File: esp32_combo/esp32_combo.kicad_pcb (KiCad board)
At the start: 2 copper layers, 90 x 43 mm, 34 parts, among them J1 TERM BLK 3.5MM 2P SIDE, J2 TERM BLK 3.5MM 6P SIDE, J3 TERM BLK 3.5MM 6P SIDE, J4 TERM BLK 3.5MM 3P SIDE, J5 TERM BLK 3.5MM 3P SIDE, J6 HDR SKT 5PIN VERT 2.54MM, J7 HDR SKT 7PIN VERT 2.54MM, J8 SKT 2x6PIN VERT 2.54MM, J9 HDR SKT 8PIN VERT 2.54MM, Q1 AS2302, SW1 SS12D10, U1 TB6612FNG Module, U2 ESP32 DEV KIT Module 30-pin, U3 LM2596 Module

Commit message: Logo
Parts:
- added G***: LOGO, Makerspet:Maker's Pet Logo 7mm, F.Cu at (58.1, 48.3)
- added G***: LOGO, Makerspet:Maker's Pet Logo 7mm, B.Cu at (120.0, 40.2)
- J7: value HDR SKT 7PIN VERT 2.54MM -> HDR SKT 6PIN VERT 2.54MM; footprint Connector_PinSocket_2.54mm:PinSocket_1x07_P2.54mm_Vertical -> Connector_PinSocket_2.54mm:PinSocket_1x06_P2.54mm_Vertical
- moved SW1 2.67 mm to (62.4, 33.4)
- moved D2 2.62 mm to (54.1, 35.3)
- moved F1 2.62 mm to (51.8, 35.2)
- moved D1 2.59 mm to (71.8, 37.0)
- moved J7 2.54 mm to (71.3, 34.0)
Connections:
- net Net-(D3-A) renamed /MOT
- J7 pad 2: GND -> +5V
- J7 pad 3: +5V -> /GPIO27
- J7 pad 4: /GPIO27 -> /GPIO18
- J7 pad 5: /GPIO18 -> /GPIO5_BOOT_STRAP
- J7 pad 6: /GPIO5_BOOT_STRAP -> /GPIO4
- J9 pad 5: Net-(J9-Pin_5) -> /LDS_PWM
- J9 pad 6: /LDS_PWM -> /LDS_EN
- J9 pad 7: /LDS_RX -> Net-(J9-Pin_7)
- J9 pad 8: /LDS_EN -> /LDS_RX
- R11 pad 2: Net-(J9-Pin_5) -> Net-(J9-Pin_7)
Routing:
- net Net-(J9-Pin_7): track 0.00 -> 32.0 mm
- net Net-(J9-Pin_5): track 27.4 -> 0.00 mm
- net /LDS_EN: track 28.3 -> 17.1 mm
- net Vdrive: track 145.3 -> 142.7 mm
- net Net-(D1-K): track 29.0 -> 31.6 mm
- net Net-(J1-Pin_1): track 6.45 -> 8.73 mm
- net /LDS_RX: track 28.4 -> 30.2 mm
- net +5V: track 242.2 -> 240.5 mm
- net /LDS_PWM: track 61.2 -> 62.6 mm
- net /GPIO27: track 27.2 -> 27.8 mm
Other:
- board text added: "- BAT +"
- board text added: "COMBO"
- board text added: "EN"
- board text added: "INT"
- board text added: "MOT"
- board text added: "R1 ©2024"
- board text added: "RX"
- board text added: "SCL"
- board text added: "SDA"
- board text added: "TX"
- board text added: "U/S SENSOR"
- board text removed: "+BAT"
- board text removed: "Combo v0.1.0"
- board text removed: "U/S DIST SENSOR"

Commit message: Combo tweaks
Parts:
- removed C2: 100uF 16V, Capacitor_Tantalum_SMD:CP_EIA-7343-15_Kemet-W
- C1: value 22uF -> 22uF 6.3V
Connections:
- net /EA_LEFT renamed /EA_LEFT_FG
- net /EA_RIGHT renamed /EA_RIGHT_FG
- net /ENC_A_LEFT renamed /ENC_A_LEFT_FG
- net /ENC_A_RIGHT renamed /ENC_A_RIGHT_FG
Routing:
- net GND: track 9.26 -> 4.78 mm
- net Vdrive: track 142.7 -> 138.7 mm
- net +5V: track 240.5 -> 244.4 mm
- net /LDS_EN: track 17.1 -> 15.9 mm
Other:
- board text added: "EA/FG"
- board text added: "FG/EA"
- board text added: "Max 13.5V 1.2A avg per motor"
- board text removed: "EA"

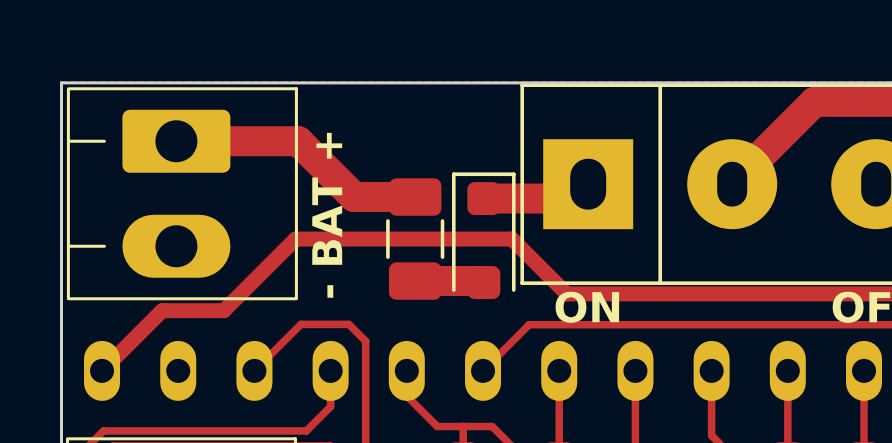
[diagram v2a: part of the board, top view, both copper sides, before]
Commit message: Fuse silkscreen
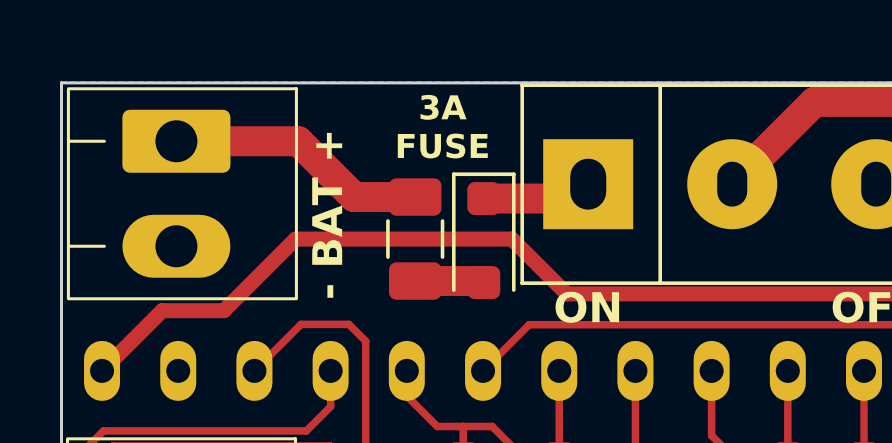
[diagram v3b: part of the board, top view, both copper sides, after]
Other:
- board text added: "3A FUSE"
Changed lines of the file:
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@@
+		)
+	)
+	(gr_text "3A\nFUSE"
+		(at 52.7 32.6 0)
+		(layer "F.SilkS" knockout)
+		(effects
+			(font
+				(size 0.8 0.8)
+				(thickness 0.15)
+				(bold yes)
+			)
+			(justify bottom)
 		)
 	)

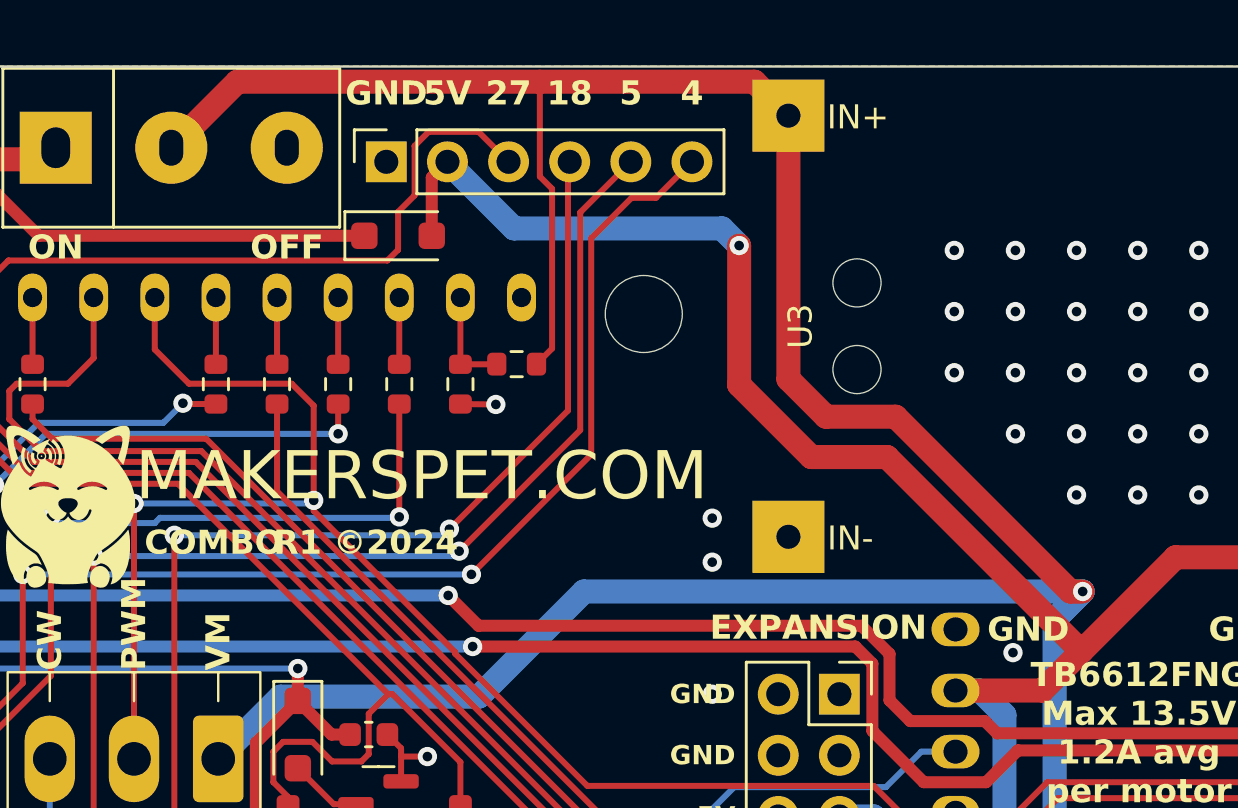
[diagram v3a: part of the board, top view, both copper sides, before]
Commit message: 3A diode
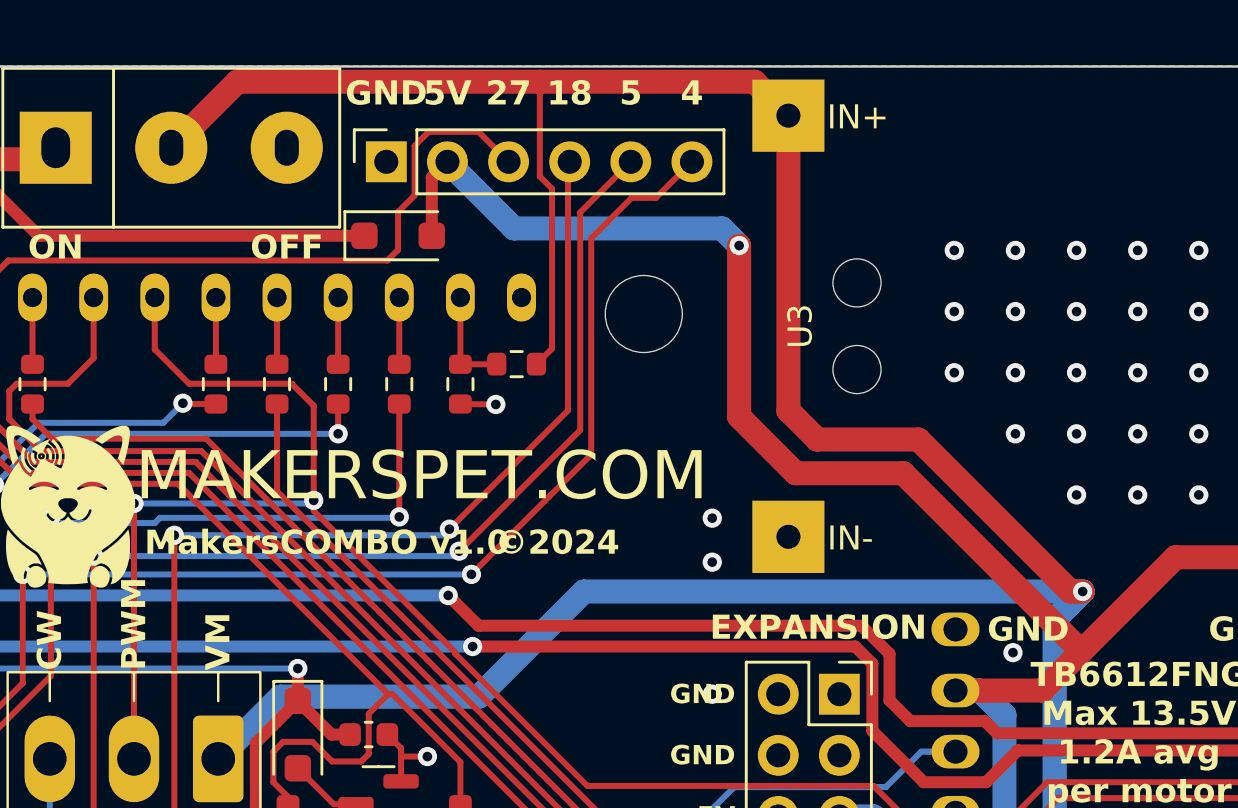
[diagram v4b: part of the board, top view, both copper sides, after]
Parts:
- D2: value FS26 -> FS36
- R5: value 200k -> 200k 1%
- R6: value 20k -> 20k 1%
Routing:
- net +5V: track 244.4 -> 245.2 mm
- net Vdrive: track 138.7 -> 139.4 mm
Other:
- board text added: "MakersCOMBO v1.0"
- board text added: "©2024"
- board text removed: "COMBO"
- board text removed: "R1 ©2024"
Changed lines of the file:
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@@
 	(paper "A5")
 	(title_block
-		(title "ESP32 Combo PCB")
-		(date "2024-04-05")
-		(rev "0.1.0")
+		(title "MakerCombo")
+		(date "2024-04-23")
+		(rev "v1.1.0")
 		(company "makerspet.com")
 	)
@@
 			)
 		)
-		(property "Value" "200k"
+		(property "Value" "200k 1%"
 			(at 0 1.43 0)
 			(layer "F.Fab")
@@
 			)
 		)
-		(property "Value" "FS26"
+		(property "Value" "FS36"
 			(at 0 2.1 90)
 			(layer "F.Fab")
@@
 			)
 		)
-		(property "Datasheet" "https://www.digikey.com/en/products/detail/good-ark-semiconductor/FS26/18667798"
+		(property "Datasheet" "https://www.digikey.com/en/products/detail/good-ark-semiconductor/FS36/18648966"
 			(at 0 0 -90)
 			(unlocked yes)
@@
 			)
 		)
-		(property "Value" "20k"
+		(property "Value" "20k 1%"
 			(at 0 1.43 90)
 			(layer "F.Fab")
@@
 		(layer "Edge.Cuts")
 	)
-	(gr_text "COMBO  "
+	(gr_text "MakersCOMBO v1.0"
 		(at 116.586 41.91 0)
 		(layer "B.SilkS" knockout)
@@
 		)
 	)
-	(gr_text "R1 ©2024"
-		(at 111.2266 41.91 0)
+	(gr_text "©2024"
+		(at 102 41.91 0)
 		(layer "B.SilkS")
 		(effects
@@
 		)
 	)
-	(gr_text "R1 ©2024"
-		(at 66.5988 50.3682 0)
+	(gr_text "©2024"
+		(at 75.8 50.3682 0)
 		(layer "F.SilkS")
 		(effects
@@
 		)
 	)
-	(gr_text "COMBO  "
+	(gr_text "MakersCOMBO v1.0"
 		(at 61.2394 50.3682 0)
 		(layer "F.SilkS" knockout)
@@
 	)
 	(segment
-		(start 73.1804 37.0332)
-		(end 73.1804 34.6122)
-		(width 0.5)
+		(start 88.3 46.9)
+		(end 92.7724 46.9)
+		(width 1)
 		(layer "F.Cu")
 		(net 1)
 	)
 	(segment
-		(start 85.9536 37.4396)
-		(end 85.9536 43.2308)
-		(width 1)
+		(start 73.1804 37.0332)
+		(end 73.1804 34.6122)
+		(width 0.5)
 		(layer "F.Cu")
 		(net 1)
@@
 	)
 	(segment
-		(start 92.1004 46.228)
-		(end 100.1776 54.3052)
-		(width 1)
-		(layer "F.Cu")
-		(net 1)
-	)
-	(segment
 		(start 51.9176 53.389)
 		(end 48.4614 53.389)
@@
 	)
 	(segment
+		(start 85.9536 37.4396)
+		(end 85.9536 44.5536)
+		(width 1)
+		(layer "F.Cu")
+		(net 1)
+	)
+	(segment
 		(start 67.1 66.6)
 		(end 66.3 66.6)
@@
 	)
 	(segment
+		(start 92.7724 46.9)
+		(end 100.1776 54.3052)
+		(width 1)
+		(layer "F.Cu")
+		(net 1)
+	)
+	(segment
 		(start 108.1024 67.9704)
 		(end 108.1024 67.31)
@@
 	)
 	(segment
-		(start 85.9536 43.2308)
-		(end 88.9508 46.228)
+		(start 85.9536 44.5536)
+		(end 88.3 46.9)
 		(width 1)
 		(layer "F.Cu")
@@
 	)
 	(segment
-		(start 88.9508 46.228)
-		(end 92.1004 46.228)
-		(width 1)
-		(layer "F.Cu")
-		(net 1)
-	)
-	(segment
 		(start 108.1024 67.31)
 		(end 106.6292 65.8368)
@@
 	)
 	(segment
-		(start 99.7204 51.816)
-		(end 92.456 44.5516)
+		(start 93.4044 45.5)
+		(end 89.2 45.5)
 		(width 1)
 		(layer "F.Cu")
@@
 	)
 	(segment
-		(start 92.456 44.5516)
-		(end 89.5604 44.5516)
+		(start 99.0654 70.9222)
+		(end 100.5332 72.39)
 		(width 1)
 		(layer "F.Cu")
@@
 	)
 	(segment
-		(start 99.0654 70.9222)
-		(end 100.5332 72.39)
+		(start 99.7204 51.816)
+		(end 93.4044 45.5)
 		(width 1)
 		(layer "F.Cu")
@@
 	)
 	(segment
-		(start 88.0008 42.992)
-		(end 88.0008 32.0424)
-		(width 1)
-		(layer "F.Cu")
-		(net 7)
-	)
-	(segment
 		(start 77.6732 30.6324)
 		(end 86.5908 30.6324)
@@
 	)
 	(segment
-		(start 100.2284 51.816)
-		(end 99.7204 51.816)
+		(start 88.0008 44.3008)
+		(end 88.0008 32.0424)
+		(width 1)
+		(layer "F.Cu")
+		(net 7)
+	)
+	(segment
+		(start 89.2 45.5)
+		(end 88.0008 44.3008)
 		(width 1)
 		(layer "F.Cu")
@@
 	)
 	(segment
-		(start 89.5604 44.5516)
-		(end 88.0008 42.992)
+		(start 99.0654 69.1436)
+		(end 99.0654 70.9222)
 		(width 1)
 		(layer "F.Cu")
@@
 	)
 	(segment
-		(start 99.0654 69.1436)
-		(end 99.0654 70.9222)
+		(start 100.2284 51.816)
+		(end 99.7204 51.816)
 		(width 1)
 		(layer "F.Cu")

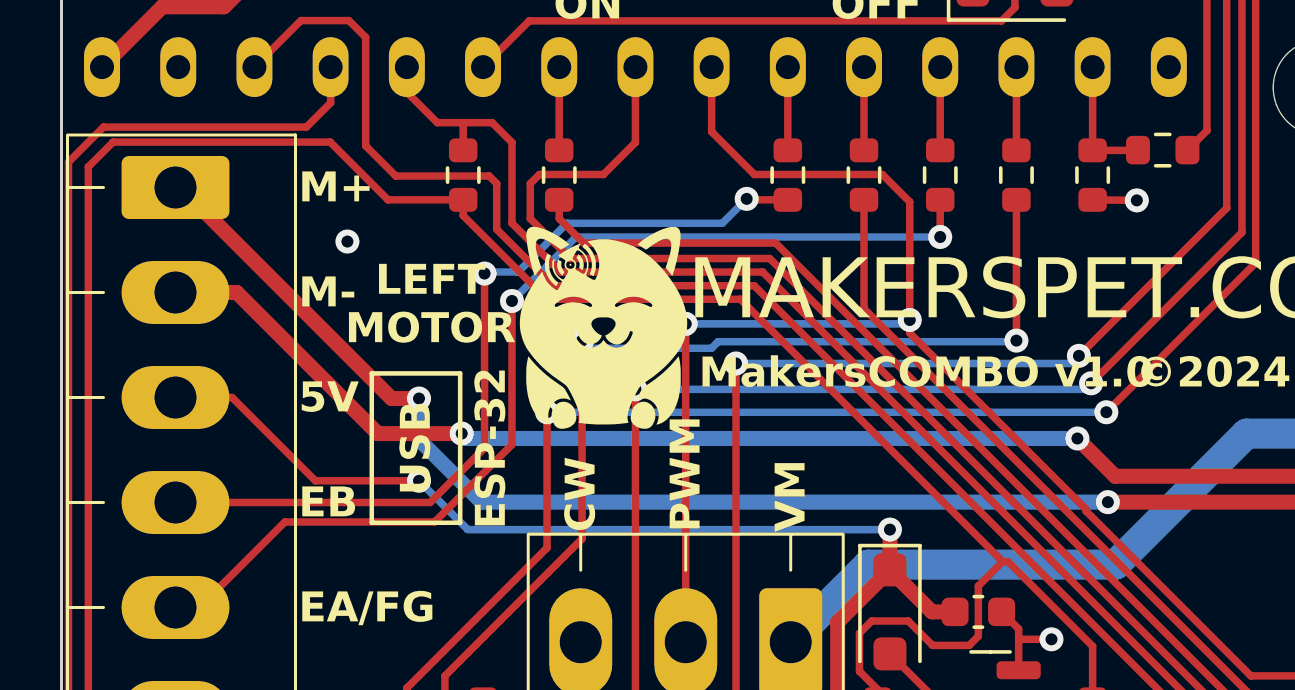
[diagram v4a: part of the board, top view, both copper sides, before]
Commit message: Motor direction bugfix
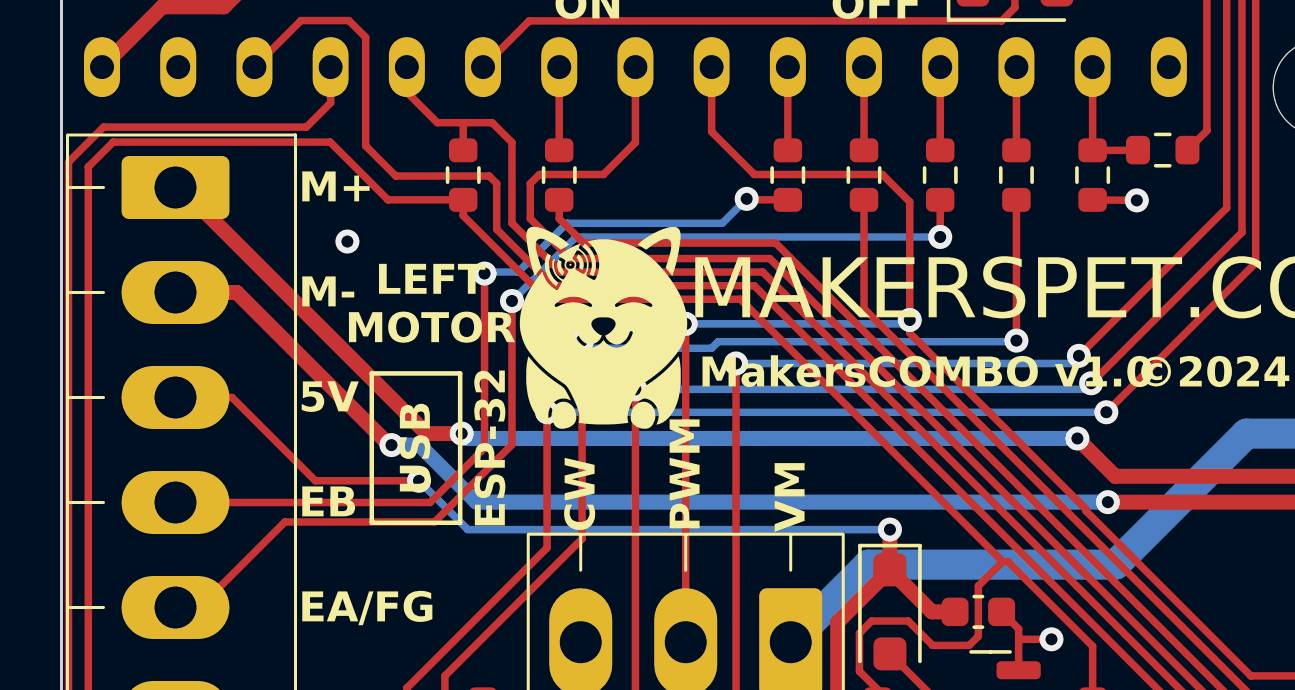
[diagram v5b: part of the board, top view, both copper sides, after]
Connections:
- U1 pad 6: /M+LEFT -> /M-LEFT
- U1 pad 7: /M-LEFT -> /M+LEFT
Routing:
- net /M+LEFT: track 76.1 -> 74.1 mm
- net /M-LEFT: track 72.6 -> 73.8 mm
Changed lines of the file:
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@@
 			(layers "*.Cu" "*.Mask")
 			(remove_unused_layers no)
-			(net 8 "/M+LEFT")
+			(net 9 "/M-LEFT")
 			(pinfunction "B02")
 			(pintype "bidirectional")
@@
 			(layers "*.Cu" "*.Mask")
 			(remove_unused_layers no)
-			(net 9 "/M-LEFT")
+			(net 8 "/M+LEFT")
 			(pinfunction "B01")
 			(pintype "passive")
@@
 	)
 	(segment
-		(start 91.4908 54.8132)
-		(end 91.4908 57.6072)
+		(start 91.0336 53.2384)
+		(end 92.202 54.4068)
 		(width 0.5)
 		(layer "F.Cu")
@@
 	)
 	(segment
-		(start 96.2152 59.7408)
-		(end 97.536 58.42)
+		(start 73.8632 51.979599)
+		(end 75.122001 53.2384)
 		(width 0.5)
 		(layer "F.Cu")
@@
 	)
 	(segment
-		(start 97.536 58.42)
-		(end 110.1344 58.42)
+		(start 96.6724 57.7088)
+		(end 108.4072 57.7088)
 		(width 0.5)
 		(layer "F.Cu")
@@
 	)
 	(segment
-		(start 74.8792 54.102)
-		(end 90.7796 54.102)
+		(start 108.4072 57.7088)
+		(end 110.1852 55.9308)
 		(width 0.5)
 		(layer "F.Cu")
@@
 	)
 	(segment
-		(start 51.9176 50.6476)
-		(end 51.8668 50.6476)
+		(start 92.202 56.3372)
+		(end 93.0656 57.2008)
 		(width 0.5)
 		(layer "F.Cu")
@@
 	)
 	(segment
-		(start 43.9691 43.6135)
-		(end 51.0032 50.6476)
+		(start 96.1644 57.2008)
+		(end 96.6724 57.7088)
 		(width 0.5)
 		(layer "F.Cu")
@@
 	)
 	(segment
-		(start 91.4908 57.6072)
-		(end 93.6244 59.7408)
+		(start 75.122001 53.2384)
+		(end 91.0336 53.2384)
 		(width 0.5)
 		(layer "F.Cu")
@@
 	)
 	(segment
-		(start 90.7796 54.102)
-		(end 91.4908 54.8132)
+		(start 92.202 54.4068)
+		(end 92.202 56.3372)
 		(width 0.5)
 		(layer "F.Cu")
@@
 	)
 	(segment
-		(start 43.8 43.6135)
-		(end 43.9691 43.6135)
+		(start 52.1716 51.816)
+		(end 53.34 51.816)
 		(width 0.5)
 		(layer "F.Cu")
@@
 	)
 	(segment
-		(start 93.6244 59.7408)
-		(end 96.2152 59.7408)
+		(start 93.0656 57.2008)
+		(end 96.1644 57.2008)
 		(width 0.5)
 		(layer "F.Cu")
@@
 	)
 	(segment
-		(start 110.1344 58.42)
-		(end 110.1852 58.4708)
+		(start 43.8 43.6135)
+		(end 43.9691 43.6135)
 		(width 0.5)
 		(layer "F.Cu")
@@
 	)
 	(segment
-		(start 51.0032 50.6476)
-		(end 51.9176 50.6476)
+		(start 43.9691 43.6135)
+		(end 52.1716 51.816)
 		(width 0.5)
 		(layer "F.Cu")
@@
 	)
 	(via
-		(at 51.9176 50.6476)
+		(at 73.8632 51.979599)
 		(size 0.8)
 		(drill 0.4)
@@
 	)
 	(via
-		(at 74.8792 54.102)
+		(at 53.34 51.816)
 		(size 0.8)
 		(drill 0.4)
@@
 	)
 	(segment
-		(start 54.0004 54.102)
-		(end 51.9176 52.0192)
-		(width 0.5)
+		(start 53.3538 51.8298)
+		(end 53.34 51.816)
+		(width 0.25)
 		(layer "B.Cu")
 		(net 8)
 	)
 	(segment
-		(start 51.9176 52.0192)
-		(end 51.9176 50.6476)
+		(start 53.503599 51.979599)
+		(end 53.3538 51.8298)
 		(width 0.5)
 		(layer "B.Cu")
@@
 	)
 	(segment
-		(start 74.8792 54.102)
-		(end 54.0004 54.102)
+		(start 73.8632 51.979599)
+		(end 53.503599 51.979599)
 		(width 0.5)
 		(layer "B.Cu")
@@
 	)
 	(segment
-		(start 91.0336 53.2384)
-		(end 92.202 54.4068)
-		(width 0.5)
-		(layer "F.Cu")
-		(net 9)
-	)
-	(segment
-		(start 45.8435 47.1135)
-		(end 43.8 47.1135)
+		(start 91.4908 54.8132)
+		(end 91.4908 57.6072)
 		(width 0.5)
 		(layer "F.Cu")
@@
 	)
 	(segment
-		(start 73.8632 51.979599)
-		(end 75.122001 53.2384)
+		(start 96.2152 59.7408)
+		(end 97.536 58.42)
 		(width 0.5)
 		(layer "F.Cu")
@@
 	)
 	(segment
-		(start 96.6724 57.7088)
-		(end 108.4072 57.7088)
+		(start 97.536 58.42)
+		(end 110.1344 58.42)
 		(width 0.5)
 		(layer "F.Cu")
@@
 	)
 	(segment
-		(start 108.4072 57.7088)
-		(end 110.1852 55.9308)
+		(start 74.8792 54.102)
+		(end 90.7796 54.102)
 		(width 0.5)
 		(layer "F.Cu")
@@
 	)
 	(segment
-		(start 92.202 56.3372)
-		(end 93.0656 57.2008)
+		(start 91.4908 57.6072)
+		(end 93.6244 59.7408)
 		(width 0.5)
 		(layer "F.Cu")
@@
 	)
 	(segment
-		(start 96.1644 57.2008)
-		(end 96.6724 57.7088)
+		(start 50.93 52.2)
+		(end 45.8435 47.1135)
 		(width 0.5)
 		(layer "F.Cu")
@@
 	)
 	(segment
-		(start 75.122001 53.2384)
-		(end 91.0336 53.2384)
+		(start 90.7796 54.102)
+		(end 91.4908 54.8132)
 		(width 0.5)
 		(layer "F.Cu")
@@
 	)
 	(segment
-		(start 92.202 54.4068)
-		(end 92.202 56.3372)
+		(start 93.6244 59.7408)
+		(end 96.2152 59.7408)
 		(width 0.5)
 		(layer "F.Cu")
@@
 	)
 	(segment
-		(start 93.0656 57.2008)
-		(end 96.1644 57.2008)
+		(start 45.8435 47.1135)
+		(end 43.8 47.1135)
 		(width 0.5)
 		(layer "F.Cu")
@@
 	)
 	(segment
-		(start 50.546 51.816)
-		(end 45.8435 47.1135)
+		(start 110.1344 58.42)
+		(end 110.1852 58.4708)
 		(width 0.5)
 		(layer "F.Cu")
@@
 	)
 	(segment
-		(start 53.34 51.816)
-		(end 50.546 51.816)
+		(start 51 52.2)
+		(end 50.93 52.2)
 		(width 0.5)
 		(layer "F.Cu")
@@
 	)
 	(via
-		(at 73.8632 51.979599)
+		(at 51 52.2)
 		(size 0.8)
 		(drill 0.4)
@@
 	)
 	(via
-		(at 53.34 51.816)
+		(at 74.8792 54.102)
 		(size 0.8)
 		(drill 0.4)
@@
 	)
 	(segment
-		(start 53.3538 51.8298)
-		(end 53.34 51.816)
-		(width 0.25)
+		(start 74.8792 54.102)
+		(end 53.832682 54.102)
+		(width 0.5)
 		(layer "B.Cu")
 		(net 9)
 	)
 	(segment
-		(start 53.503599 51.979599)
-		(end 53.3538 51.8298)
+		(start 53.832682 54.102)
+		(end 51.930682 52.2)
 		(width 0.5)
 		(layer "B.Cu")
@@
 	)
 	(segment
-		(start 73.8632 51.979599)
-		(end 53.503599 51.979599)
+		(start 51.930682 52.2)
+		(end 51 52.2)
 		(width 0.5)
 		(layer "B.Cu")
